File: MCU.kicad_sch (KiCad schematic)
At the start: 29 parts, among them J1 USB_C_Receptacle_USB2.0_16P, J5 DE9_Receptacle_MountingHoles, Q1 BC817, SW1 SW_SPST, SW2 SW_SPST, U1 ESP32-S3-MINI-1U, U2 MAX3232, U6 W25Q128JVS

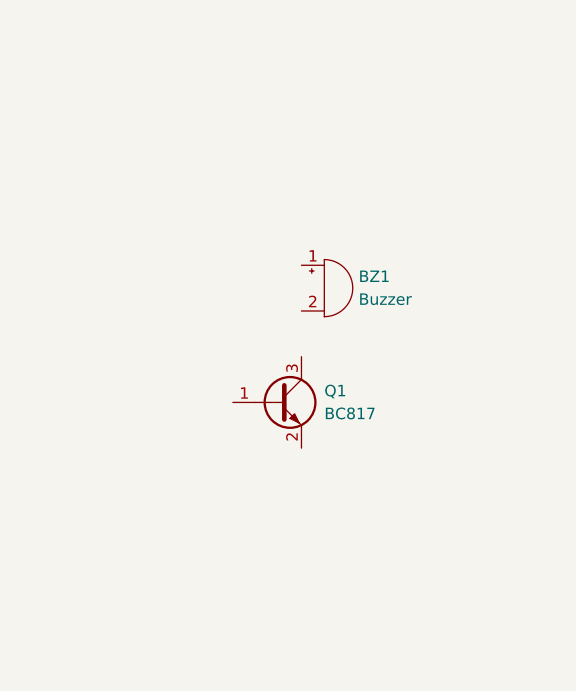
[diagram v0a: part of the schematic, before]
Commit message: buzzer sch connections
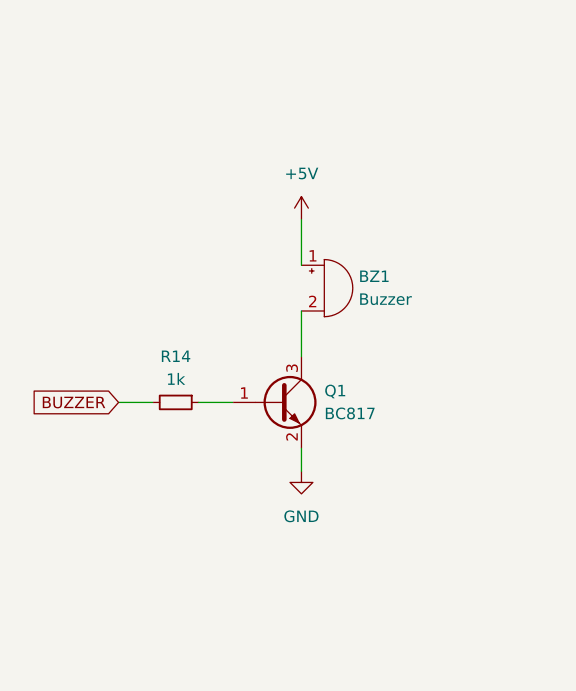
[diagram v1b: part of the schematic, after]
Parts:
- added R14: 1k, symbol Device:R_Small
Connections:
- net +5V: now also BZ1.1 (+)
- net BUZZER: now also R14.2
- net GND: now also Q1.2 (E)
- net at BZ1.2 (-): now also Q1.3 (C)
- net at Q1.1 (B): now also R14.1

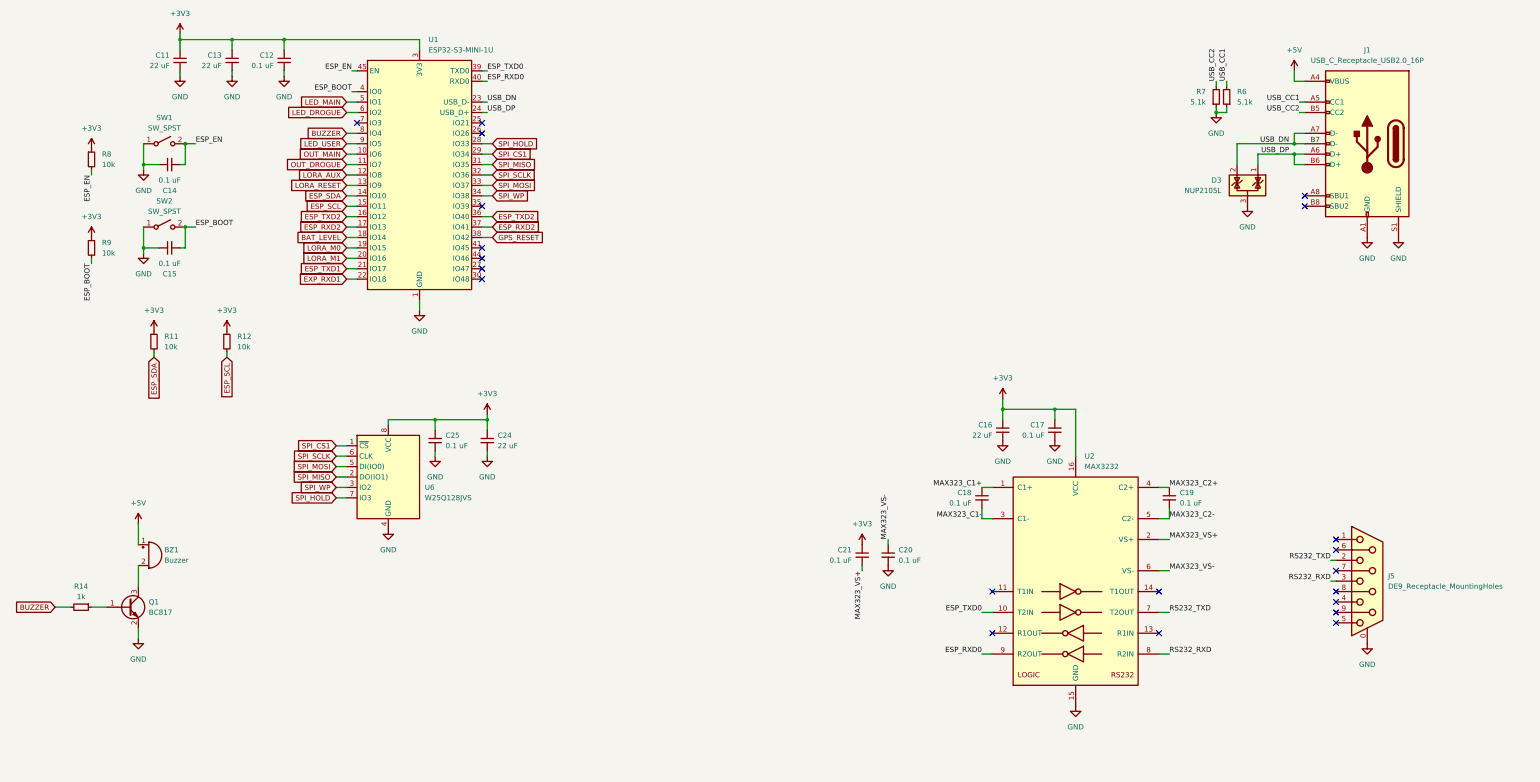
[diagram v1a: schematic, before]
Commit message: Wired barometers and GPS up, added misc LEDs, tidy-up
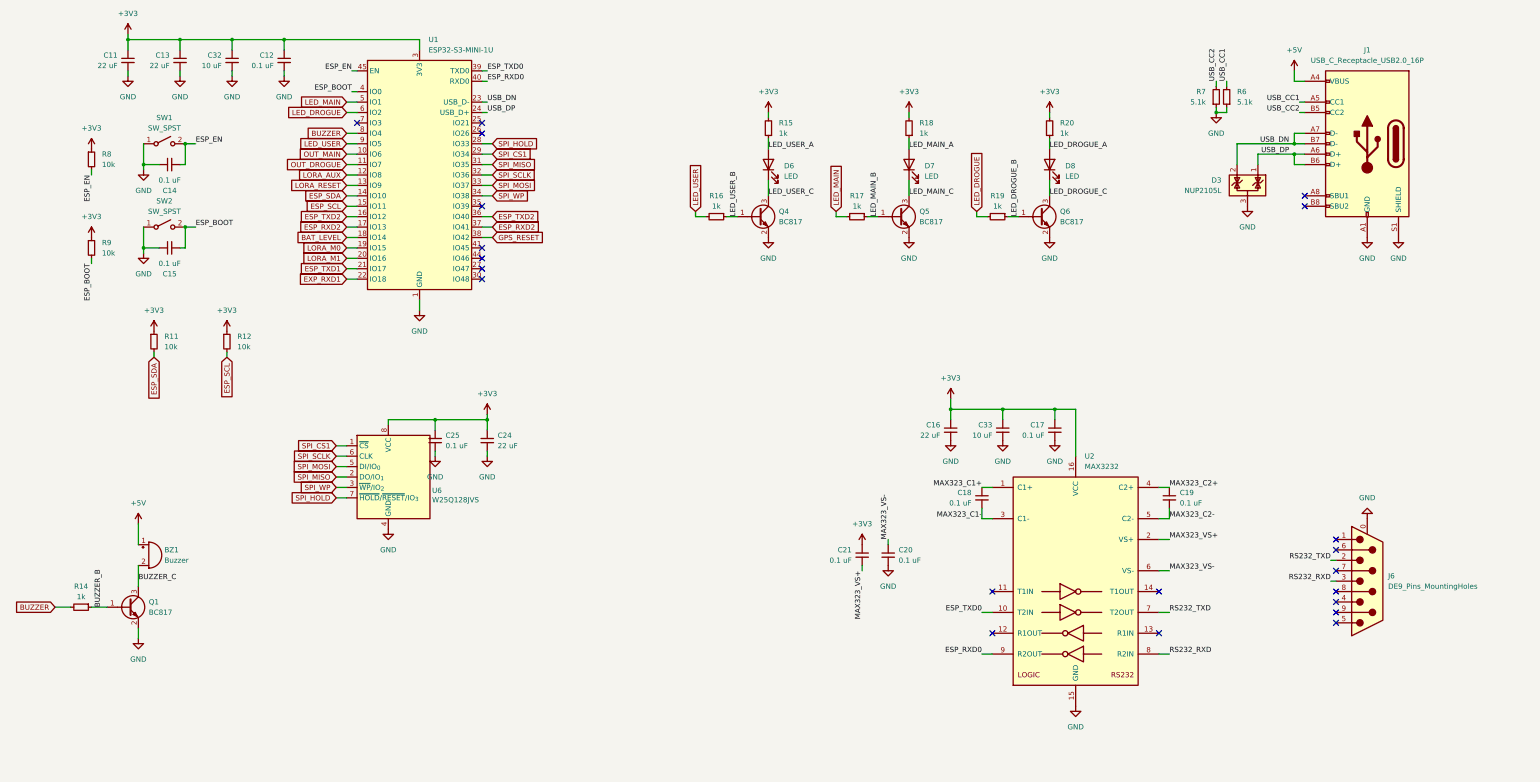
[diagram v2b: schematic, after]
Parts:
- removed J5: DE9_Receptacle_MountingHoles, Connector_Dsub:DSUB-9_Female_Horizontal_P2.77x2.84mm_EdgePinOffset7.70mm_Housed_MountingHolesOffset9.12mm, symbol Connector:DE9_Receptacle_MountingHoles
- added C32, C33: 10 uF, symbol Device:C_Small
- added D6, D7, D8: LED, LED_SMD:LED_0805_2012Metric, symbol Device:LED
- added J6: DE9_Pins_MountingHoles, Connector_Dsub:DSUB-9_Pins_Horizontal_P2.77x2.84mm_EdgePinOffset7.70mm_Housed_MountingHolesOffset9.12mm, symbol Connector:DE9_Pins_MountingHoles
- added Q4, Q5, Q6: BC817, Package_TO_SOT_SMD:SOT-23, symbol Transistor_BJT:BC817
- added R15, R16, R17, R18, R19, R20: 1k, symbol Device:R_Small
- U6: footprint Package_SO:SOIC-8_5.23x5.23mm_P1.27mm -> Package_SO:SOIC-8_5.3x5.3mm_P1.27mm
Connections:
- net +3V3: now also C32.1, C33.1, R15.2, R18.2, R20.2
- net GND: now also C32.2, C33.2, J6.0 (PAD), Q4.2 (E), Q5.2 (E), Q6.2 (E)
- net LED_DROGUE: now also R19.2
- net LED_MAIN: now also R17.2
- net LED_USER: now also R16.2
- net RS232_RXD: now also J6.3
- net RS232_TXD: now also J6.2
- net BUZZER_C: now reaches BZ1.2 (-), Q1.3 (C)
- net BUZZER_B: now reaches Q1.1 (B), R14.1
- new net LED_DROGUE_A: D8.2 (A), R20.1
- new net LED_DROGUE_B: Q6.1 (B), R19.1
- new net LED_DROGUE_C: D8.1 (K), Q6.3 (C)
- new net LED_MAIN_A: D7.2 (A), R18.1
- new net LED_MAIN_B: Q5.1 (B), R17.1
- new net LED_MAIN_C: D7.1 (K), Q5.3 (C)
- new net LED_USER_A: D6.2 (A), R15.1
- new net LED_USER_B: Q4.1 (B), R16.1
- new net LED_USER_C: D6.1 (K), Q4.3 (C)
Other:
- moved on the sheet: C11, C13, C16, U6

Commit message: preliminary schematic wired, all footprints assigned, all laid out in PCB editor.
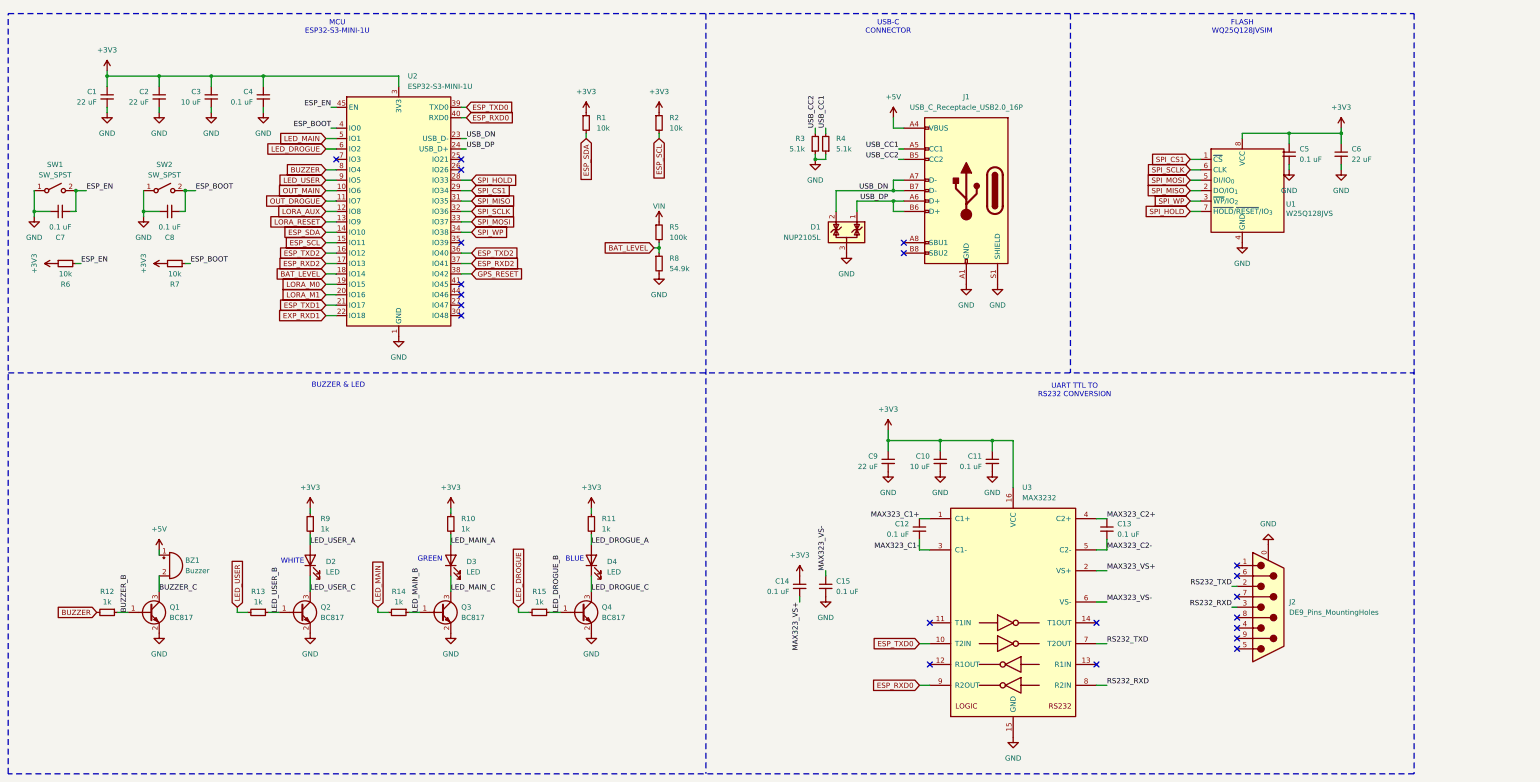
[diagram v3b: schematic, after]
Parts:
- added R5: 100k, Resistor_SMD:R_0603_1608Metric, symbol Device:R_Small
- added R8: 54.9k, Resistor_SMD:R_0603_1608Metric, symbol Device:R_Small
- C1: renamed from C11; footprint (none) -> Capacitor_SMD:C_0603_1608Metric
- C10: renamed from C33; footprint (none) -> Capacitor_SMD:C_0603_1608Metric
- C2: renamed from C13; footprint (none) -> Capacitor_SMD:C_0603_1608Metric
- C3: renamed from C32; footprint (none) -> Capacitor_SMD:C_0603_1608Metric
- C6: renamed from C24; footprint (none) -> Capacitor_SMD:C_0603_1608Metric
- C7: renamed from C14; footprint (none) -> Capacitor_SMD:C_0603_1608Metric
- C8: renamed from C15; footprint (none) -> Capacitor_SMD:C_0603_1608Metric
- C9: renamed from C16; footprint (none) -> Capacitor_SMD:C_0603_1608Metric
- R1: renamed from R11; footprint (none) -> Resistor_SMD:R_0603_1608Metric
- R10: renamed from R18; footprint (none) -> Resistor_SMD:R_0603_1608Metric
- R11: renamed from R20; footprint (none) -> Resistor_SMD:R_0603_1608Metric
- R12: renamed from R14; footprint (none) -> Resistor_SMD:R_0603_1608Metric
- R13: renamed from R16; footprint (none) -> Resistor_SMD:R_0603_1608Metric
- R14: renamed from R17; footprint (none) -> Resistor_SMD:R_0603_1608Metric
- R15: renamed from R19; footprint (none) -> Resistor_SMD:R_0603_1608Metric
- R2: renamed from R12; footprint (none) -> Resistor_SMD:R_0603_1608Metric
- R3: renamed from R7; footprint (none) -> Resistor_SMD:R_0603_1608Metric
- R4: renamed from R6; footprint (none) -> Resistor_SMD:R_0603_1608Metric
- R6: renamed from R8; footprint (none) -> Resistor_SMD:R_0603_1608Metric
- R7: renamed from R9; footprint (none) -> Resistor_SMD:R_0603_1608Metric
- R9: renamed from R15; footprint (none) -> Resistor_SMD:R_0603_1608Metric
- renumbered C17 to C11, C18 to C12, C19 to C13, C21 to C14, C20 to C15, C12 to C4, C25 to C5, D3 to D1, D6 to D2, D7 to D3, D8 to D4, J6 to J2, Q4 to Q2, Q5 to Q3, Q6 to Q4, U6 to U1, U1 to U2, U2 to U3
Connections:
- net +3V3: now also R7.2; no longer R7.1
- net BAT_LEVEL: now also R5.2, R8.1
- net ESP_BOOT: now also R7.1; no longer R7.2
- net GND: now also R8.2
- new net VIN: R5.1
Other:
- note added: "BLUE"
- note added: "BUZZER & LED"
- note added: "FLASH WQ25Q128JVSIM"
- note added: "GREEN"
- note added: "MCU ESP32-S3-MINI-1U"
- note added: "UART TTL TO RS232 CONVERSION"
- note added: "USB-C CONNECTOR"
- note added: "WHITE"
- moved on the sheet: BZ1, C1, C10, C11, C12, C13, C14, C15, C2, C3, C4, C5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

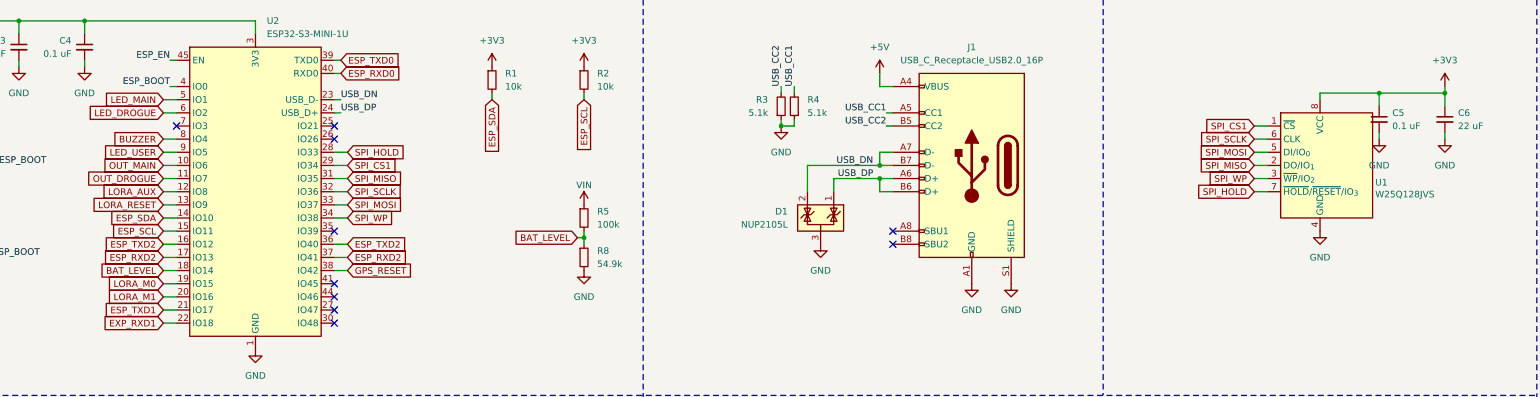
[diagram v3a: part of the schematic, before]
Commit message: reassigned some footprints, preliminary PCB layout
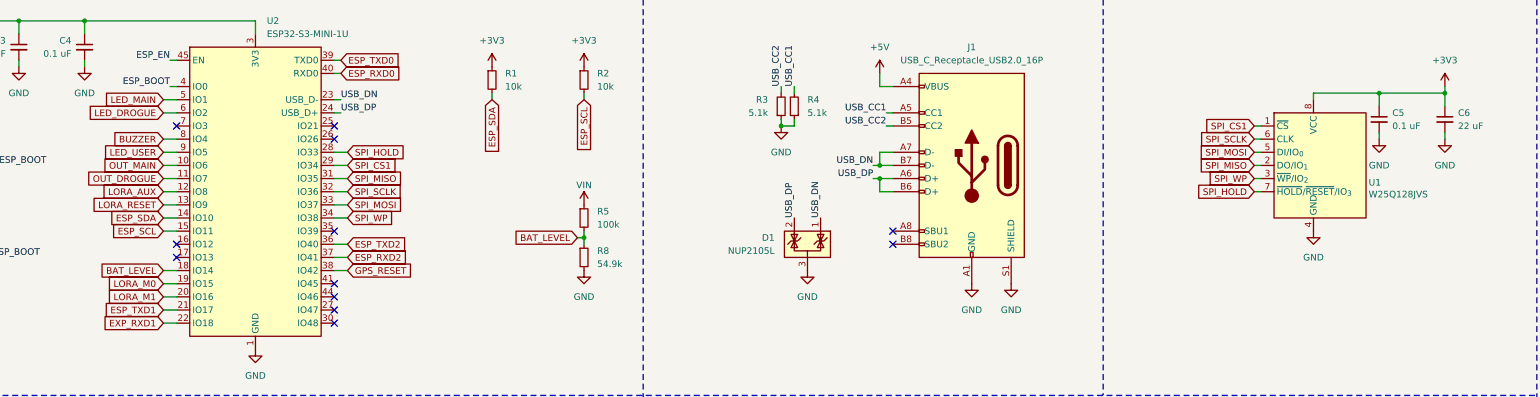
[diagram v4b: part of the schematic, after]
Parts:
- C11, C12, C13, C14, C15, C4, C5: footprint Capacitor_SMD:C_0805_2012Metric -> Capacitor_SMD:C_0603_1608Metric
- D2, D3, D4: footprint LED_SMD:LED_0805_2012Metric -> LED_SMD:LED_0603_1608Metric
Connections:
- net ESP_RXD2: no longer U2.17 (IO13)
- net ESP_TXD2: no longer U2.16 (IO12)
- net USB_DN: now also D1.1 (K); no longer D1.2 (K)
- net USB_DP: now also D1.2 (K); no longer D1.1 (K)
- no-connect marks 21 -> 23
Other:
- moved on the sheet: D1, U1

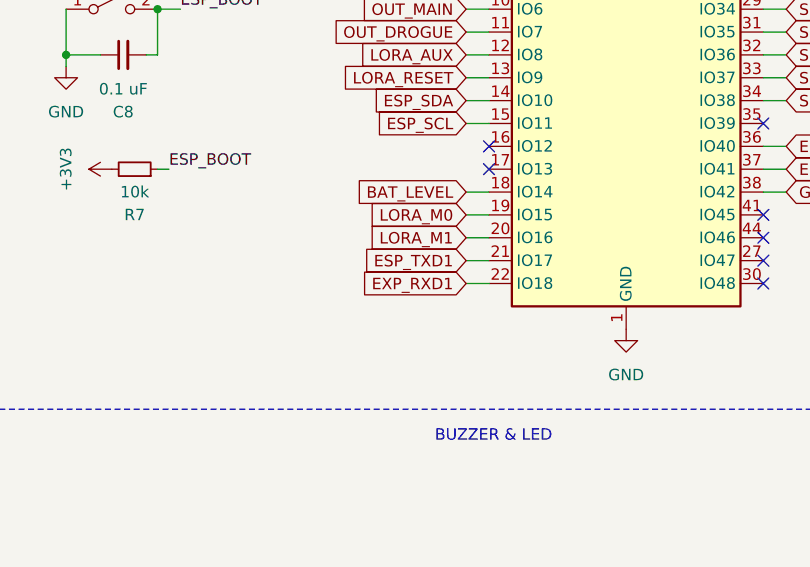
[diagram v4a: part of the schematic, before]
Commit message: added missing output diodes, added 3d models, misc. re-laying
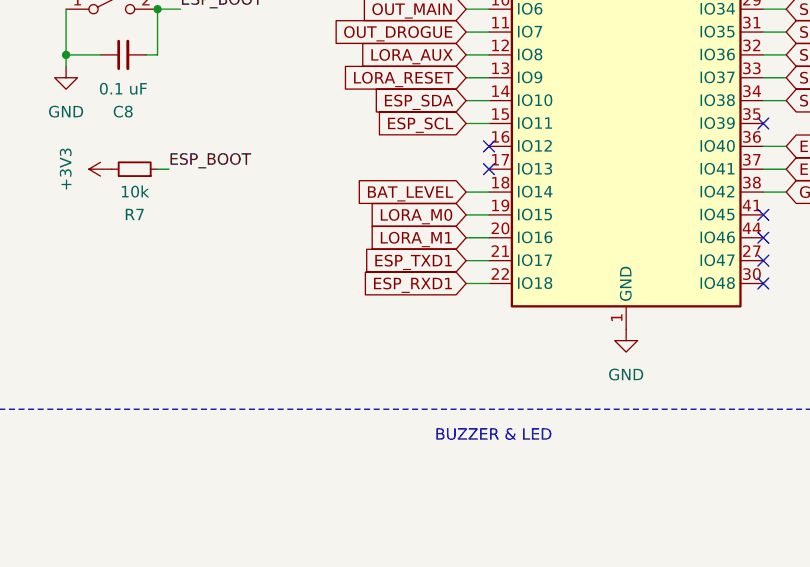
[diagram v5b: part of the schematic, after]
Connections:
- net EXP_RXD1 renamed ESP_RXD1
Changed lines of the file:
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@@
 		)
 	)
-	(global_label "EXP_RXD1"
+	(global_label "ESP_RXD1"
 		(shape input)
 		(at 100.33 93.98 180)
@@
 		(dnp no)
 		(fields_autoplaced yes)
-		(property "Reference" "#PWR017"
+		(property "Reference" "#PWR020"
 			(at 224.79 90.17 0)
 			(effects
@@
 			(project "valkyriev3"
 				(path "/d24fd15c-a242-4d26-9876-7755ca0d378c/d62cb9a5-57b0-46af-b3af-5759837aeb39"
-					(reference "#PWR017")
+					(reference "#PWR020")
 					(unit 1)
 				)
@@
 		(dnp no)
 		(fields_autoplaced yes)
-		(property "Reference" "#PWR019"
+		(property "Reference" "#PWR018"
 			(at 64.77 81.28 0)
 			(effects
@@
 			(project "valkyriev3"
 				(path "/d24fd15c-a242-4d26-9876-7755ca0d378c/d62cb9a5-57b0-46af-b3af-5759837aeb39"
-					(reference "#PWR019")
+					(reference "#PWR018")
 					(unit 1)
 				)
@@
 		(dnp no)
 		(fields_autoplaced yes)
-		(property "Reference" "#PWR020"
+		(property "Reference" "#PWR019"
 			(at 181.61 90.17 0)
 			(effects
@@
 			(project "valkyriev3"
 				(path "/d24fd15c-a242-4d26-9876-7755ca0d378c/d62cb9a5-57b0-46af-b3af-5759837aeb39"
-					(reference "#PWR020")
+					(reference "#PWR019")
 					(unit 1)
 				)
@@
 		(dnp no)
 		(fields_autoplaced yes)
-		(property "Reference" "#PWR018"
+		(property "Reference" "#PWR017"
 			(at 38.1 81.28 0)
 			(effects
@@
 			(project "valkyriev3"
 				(path "/d24fd15c-a242-4d26-9876-7755ca0d378c/d62cb9a5-57b0-46af-b3af-5759837aeb39"
-					(reference "#PWR018")
+					(reference "#PWR017")
 					(unit 1)
 				)
